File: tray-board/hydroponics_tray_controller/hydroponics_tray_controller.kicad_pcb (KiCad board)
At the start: 2 copper layers, 99.5 x 99.5 mm, 30 parts, among them J1 Jumper, J2 Display_Connector_Touch, J3 SD_Connector, J4 Power_Comms, J5 i2c_Peripherals, J6 1Wire_Peripherals, SW1 RotaryEncoder_Switch, U1 ESP32, U2 SP3485EN, U3 AMS1117-3.3

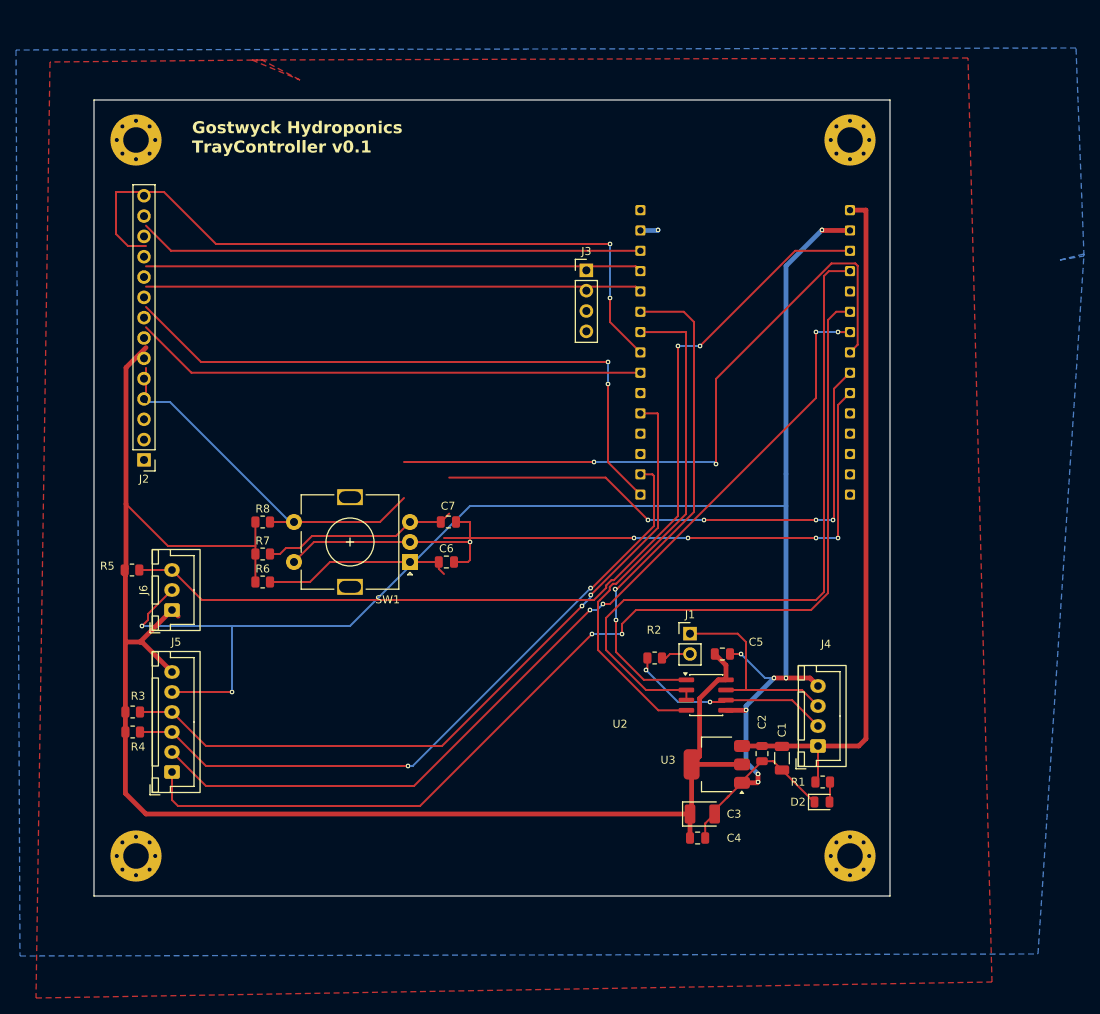
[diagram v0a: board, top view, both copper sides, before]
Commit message: tray-board: merge display+SD connector into one symbol, fix SD pad position, re-sync PCB
- New_Library: merged the 14-pin main header and 4-pin SD header into a
  single Display_MSP2401_2.4in_Touch schematic symbol, matching the combined
  footprint's fixed connector spacing. J3 (standalone SD connector) removed;
  its nets are now carried by the merged symbol's SD1-SD4 pins.
- Footprint: fixed SD1-SD4 pad Y-coordinate (6.51mm -> 3.00mm from the top
  edge) - they sit in the same row as the two top mounting holes, per the
  mechanical drawing.
- Fixed H1-H4 mounting hole footprint (MountingHole_3.2mm_M3_Pad_Via ->
  MountingHole_3.2mm_M3) to match their "no connection" schematic symbol.
- kicad_pcb re-synced from schematic (Update PCB from Schematic + footprint
  reload) - layout/routing still in progress.

Co-Authored-By: Claude Sonnet 5 <noreply@anthropic.com>
Claude-Session: https://claude.ai/code/session_01QYbZEgBzGJ6rSai1ie8nG1
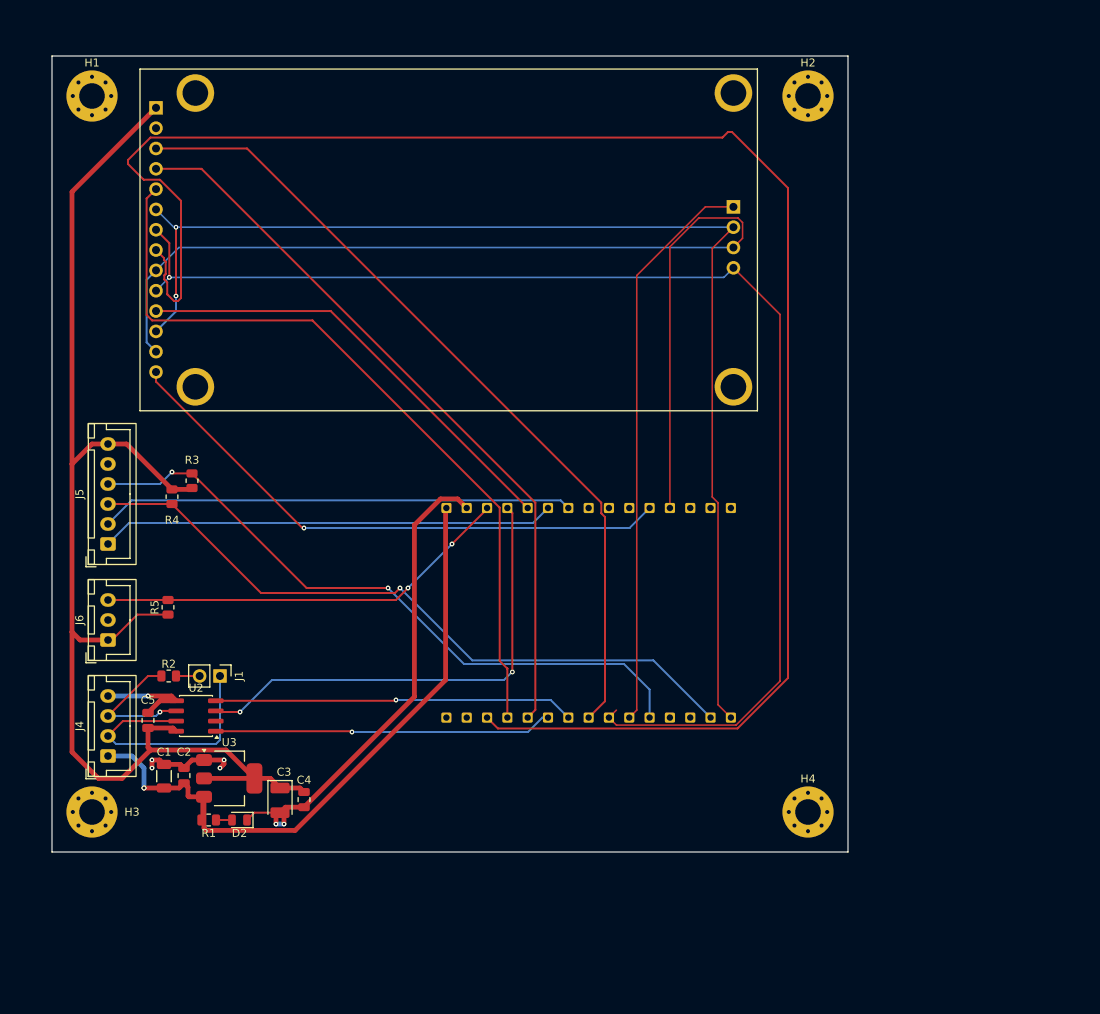
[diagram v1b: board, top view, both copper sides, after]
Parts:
- removed C6, C7: 100nF, Capacitor_SMD:C_0805_2012Metric
- removed J3: SD_Connector, Connector_PinHeader_2.54mm:PinHeader_1x04_P2.54mm_Vertical
- removed R6, R7, R8: 10k, Resistor_SMD:R_0805_2012Metric
- removed SW1: RotaryEncoder_Switch, Rotary_Encoder:RotaryEncoder_Alps_EC11E-Switch_Vertical_H20mm
- J2: value Display_Connector_Touch -> Display_MSP2401_2.4in_Touch; footprint Connector_PinHeader_2.54mm:PinHeader_1x14_P2.54mm_Vertical -> Library:Display_MSP2401_2.4in_Touch
- moved J2 90.9 mm to (108.2, 21.6), turned to -90 degrees
- moved J4 88.8 mm to (27.0, 107.5)
- moved C1 77.3 mm to (34.0, 110.0), turned to 90 degrees
- moved R1 76.9 mm to (39.6, 115.5)
- moved D2 72.8 mm to (43.4, 115.5), turned to 180 degrees
- moved C2 72.3 mm to (36.5, 110.0), turned to 90 degrees
- moved C5 72.3 mm to (32.0, 103.0), turned to 90 degrees
- moved U2 63.8 mm to (38.0, 102.5), turned to 180 degrees
- moved U3 61.0 mm to (42.1, 110.3), turned to 0 degrees
- moved R2 60.8 mm to (34.6, 97.5)
- moved J1 59.0 mm to (41.0, 97.5), turned to -90 degrees
- moved C3 52.8 mm to (48.5, 113.0), turned to -90 degrees
- moved C4 49.4 mm to (51.5, 113.0), turned to -90 degrees
- moved R3 29.8 mm to (37.5, 73.1), turned to 90 degrees
- moved R4 29.8 mm to (35.0, 75.1), turned to -90 degrees
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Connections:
- J4 pad 2: /RS485_A -> /RS485_B
- J4 pad 3: /RS485_B -> /RS485_A
- U1 pad 30: (no net) -> unconnected-(U1-EN-Pad30)
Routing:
- net GND: track 284.5 -> 86.3 mm, vias 12 -> 7
- net /ESP32_D15: track 63.1 -> 218.6 mm
- net /ESP32_D34: track 0.00 -> 131.5 mm
- net /ESP32_D25: track 102.8 -> 0.00 mm, vias 2 -> 0
- net /ESP32_D18: track 64.2 -> 159.5 mm, vias 0 -> 1
- net /ESP32_D33: track 94.0 -> 0.00 mm, vias 4 -> 0
- net /ESP32_D32: track 91.9 -> 0.00 mm, vias 4 -> 0
- net /TOF_XSHUT_2: track 134.9 -> 56.9 mm, vias 2 -> 0
- net /ESP32_D23: track 78.9 -> 150.5 mm
- net /ESP32_D35: track 0.00 -> 71.3 mm, vias 0 -> 1
- net /ESP32_D19: track 0.00 -> 71.3 mm
- net /ONEWIRE_DATA: track 121.3 -> 52.2 mm
- net /ESP32_D14: track 0.00 -> 56.7 mm
- net /TOF_XSHUT_1: track 114.9 -> 59.2 mm, vias 4 -> 0
- net +3V3: track 200.8 -> 163.9 mm
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- removed copper zone on B.Cu, net GND
- removed copper zone on F.Cu, net GND
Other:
- board text removed: "Gostwyck Hydroponics TrayController v0.1"

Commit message: tray-board: re-sync PCB, set min_clearance to 0.0
Co-Authored-By: Claude Sonnet 5 <noreply@anthropic.com>
Claude-Session: https://claude.ai/code/session_01VxeU7RBY2UcBHFLNmCs7rA
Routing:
- net /ESP32_D15: track 218.6 -> 115.0 mm
- net /ONEWIRE_DATA: track 52.2 -> 59.3 mm, vias 2 -> 0
- net GND: track 86.3 -> 92.5 mm, vias 7 -> 6
- net /ESP32_D23: track 150.5 -> 154.9 mm, vias 2 -> 1
- net /ESP32_D2: track 97.0 -> 93.1 mm
- net /ESP32_D34: track 131.5 -> 129.8 mm
- net /ESP32_D18: track 159.5 -> 158.1 mm
- net /ESP32_D12: track 60.0 -> 61.2 mm
- net /ESP32_RX2: track 42.3 -> 43.4 mm
- net /ESP32_D5: track 101.9 -> 101.2 mm
- net +5V: track 83.9 -> 83.2 mm, vias 2 -> 1
- net /TOF_XSHUT_2: track 56.9 -> 57.2 mm, vias 0 -> 2
- net /TOF_XSHUT_1: vias 0 -> 2
- net /ESP32_D14: vias 0 -> 1
- added copper zone on F.Cu, net (none)
- added copper zone on B.Cu, net GND

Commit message: tray-board: ground plane fix, stitching, C3 ceramic swap, full JLC BOM
- F.Cu ground zone was netless with island-removal off, filling as ~26
  isolated islands (DRC isolated_copper). Assigned to GND, islands removed.
- Added ~18 GND stitching vias (ICs, decoupling caps, ESP32 centreline).
- Mounting holes H1-H4 swapped to MountingHole_Pad symbols wired to GND;
  the _Pad_Via footprints now bond both pours at all four corners.
- C3 changed from 10uF tantalum (EIA-3528-21, JLC Extended) to 10uF 25V
  X5R 0805 ceramic (C15850, Basic) - board is now Basic-only.
- Populated LCSC part numbers for all 13 SMD parts, stock/Basic-checked.
- Restored the board silkscreen title dropped in the earlier re-sync.
- kicad_pro: zone default min_clearance.

ERC / DRC / schematic-parity all clean.

Co-Authored-By: Claude Sonnet 5 <noreply@anthropic.com>
Claude-Session: https://claude.ai/code/session_01AfKCQW2p52QuPuRZiddque
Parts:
- C3: footprint Capacitor_Tantalum_SMD:CP_EIA-3528-21_Kemet-B -> Capacitor_SMD:C_0805_2012Metric
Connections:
- H1 pad 1: (no net) -> GND
- H2 pad 1: (no net) -> GND
- H3 pad 1: (no net) -> GND
- H4 pad 1: (no net) -> GND
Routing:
- net GND: vias 6 -> 18
- added copper zone on F.Cu, net GND
- removed copper zone on F.Cu, net (none)
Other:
- board text added: "Gostwyck Hydroponics Tray Controller v0.1"

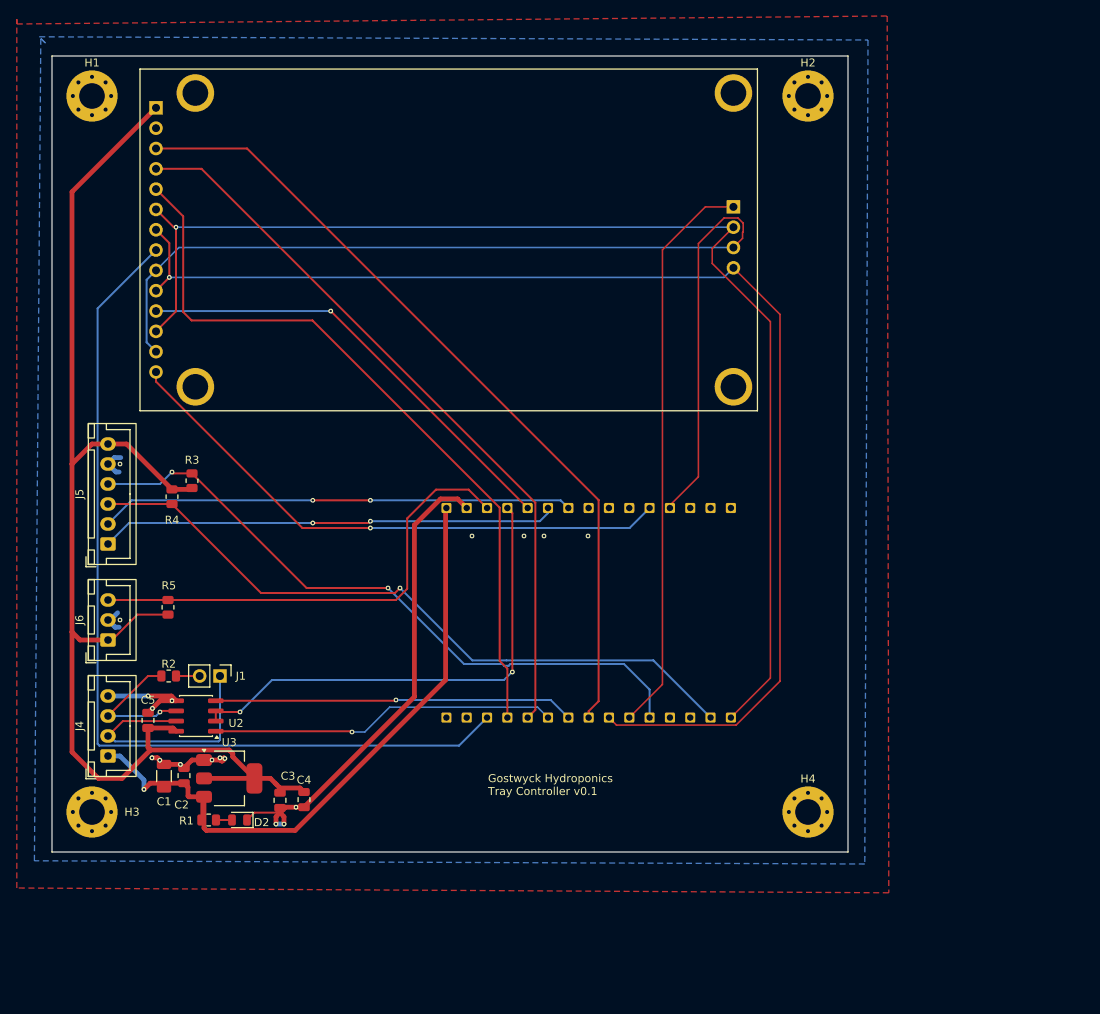
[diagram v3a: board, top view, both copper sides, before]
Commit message: tray-board: rework ESP32 socket footprint - 1.0mm holes, silk, 3D model
The ESP32 DevKit socket footprint was 30 bare pads with 0.8mm holes - too
tight for ~0.64mm header pins once splay + fab tolerance are added, and the
module (a wider 26.2mm-row variant, not the 25.4mm DOIT standard) barely fits.

- Holes 0.8 -> 1.0mm, pads 1.27 -> 1.6mm.
- Row spacing kept at 26.2mm (measured off the physical module).
- Added pin-1 square pad + silk chevron, silk row marks, F.Fab outline,
  F.CrtYd courtyard (sized to the pad field + margin).
- attr back to through_hole (had drifted to smd - same bug as a7a317e).
- 3D model wired in via a portable ${KIPRJMOD}/../../models/ path.
- ESP32 area rerouted for the larger pads.
- models/: STEP models for the ESP32 DevKit and the 2.4" display, for
  mechanical CAD. Display model not yet referenced from its footprint.

ERC / DRC / schematic-parity clean; full fab set regenerated.

Co-Authored-By: Claude Sonnet 5 <noreply@anthropic.com>
Claude-Session: https://claude.ai/code/session_01AfKCQW2p52QuPuRZiddque
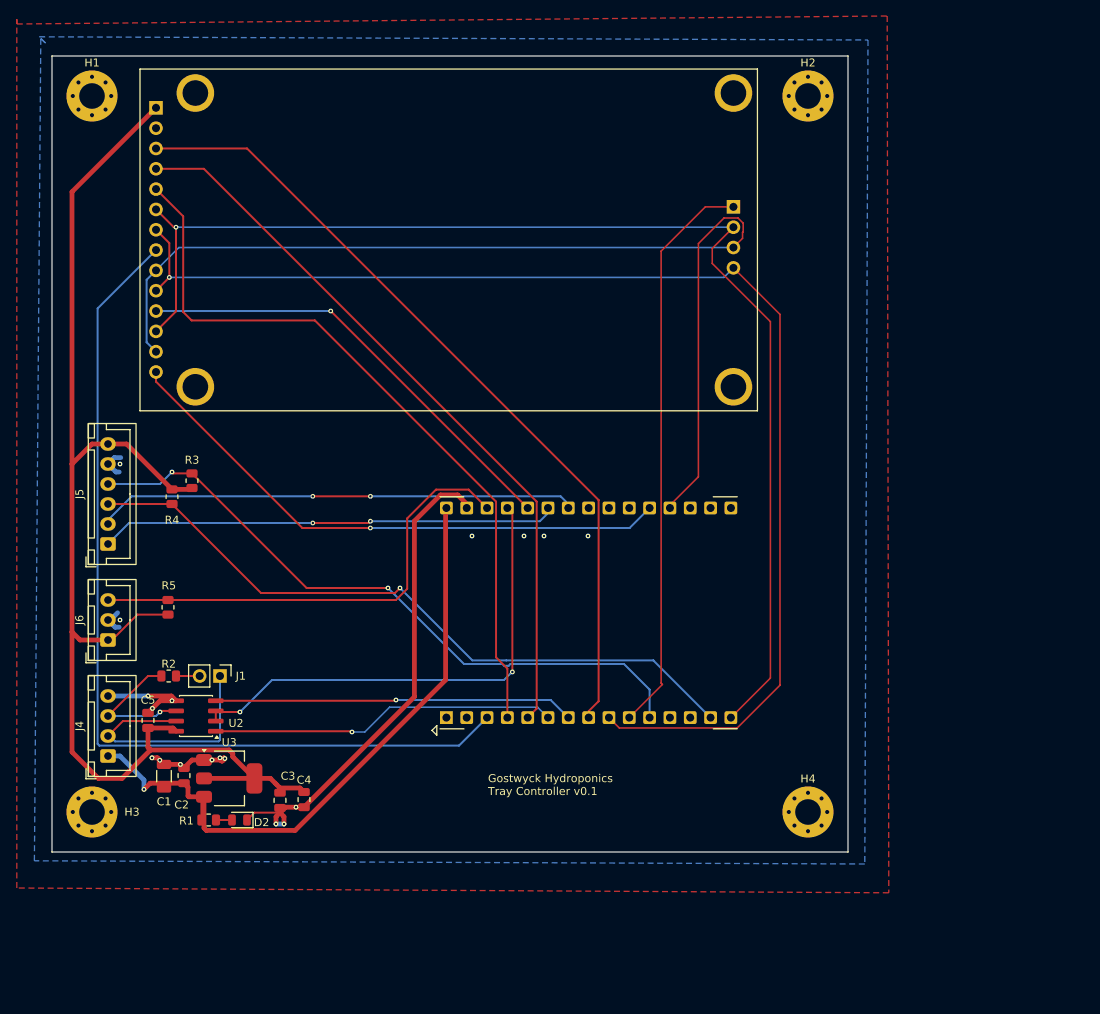
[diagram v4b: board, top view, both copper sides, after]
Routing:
- net GND: track 92.5 -> 93.5 mm
- net /ESP32_D18: track 158.1 -> 158.7 mm
